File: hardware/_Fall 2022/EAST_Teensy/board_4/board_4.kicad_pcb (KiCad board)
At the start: 2 copper layers, 7 parts, among them J1 Conn_01x04, J2 Conn_02x08_Odd_Even, U1 Teensy4.1

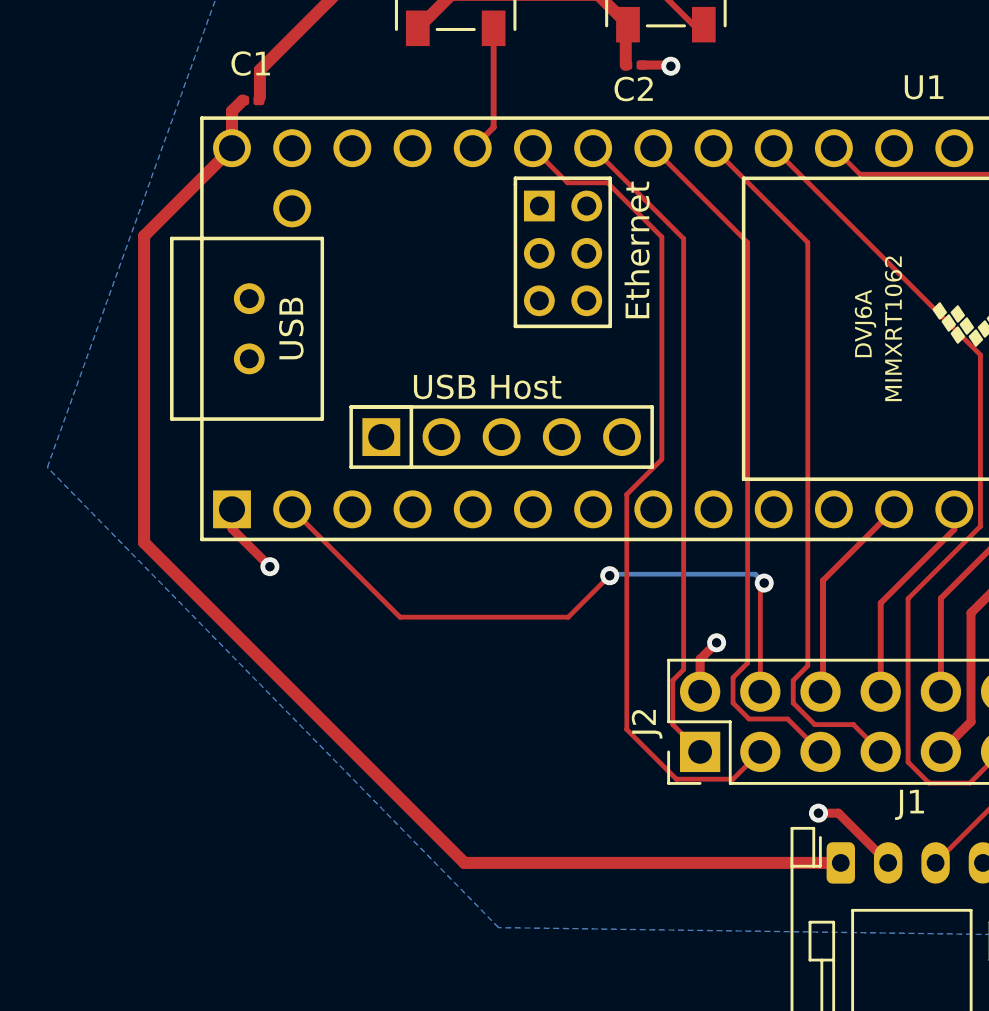
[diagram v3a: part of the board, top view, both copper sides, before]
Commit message: Edit layout of board 4
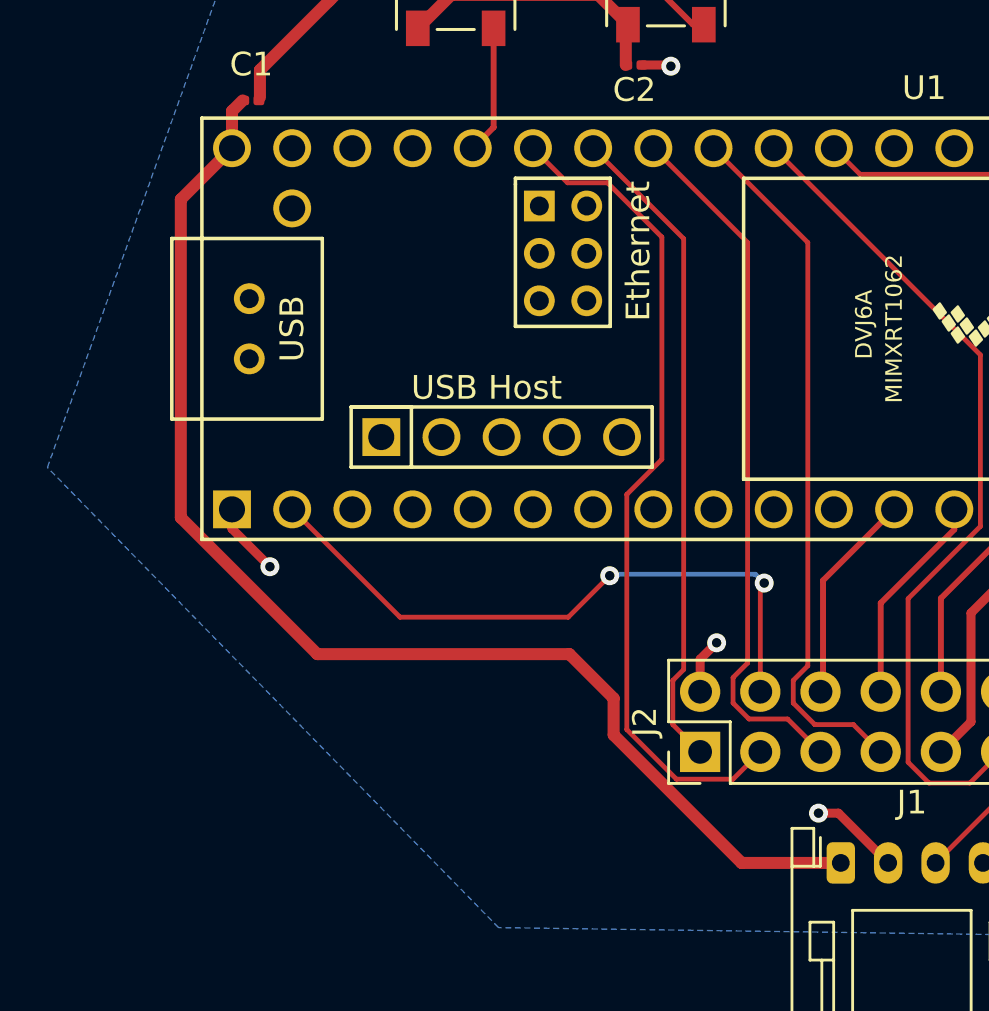
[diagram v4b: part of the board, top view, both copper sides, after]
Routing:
- net /V_BATT: track 55.4 -> 53.5 mm
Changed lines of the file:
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@@
   (gr_line (start 122.698438 153) (end 173.1 153) (layer "Dwgs.User") (width 0.2))
   (gr_circle (center 175.394719 140.299534) (end 173.565919 140.299534) (layer "Dwgs.User") (width 0.2) (fill none))
-  (segment (start 115.7 131.63) (end 115.7 118.7) (width 0.508) (layer "F.Cu") (net 1))
-  (segment (start 145.1 145.15) (end 129.22 145.15) (width 0.508) (layer "F.Cu") (net 1))
-  (segment (start 129.22 145.15) (end 115.7 131.63) (width 0.508) (layer "F.Cu") (net 1))
+  (segment (start 145.1 145.15) (end 140.914263 145.15) (width 0.508) (layer "F.Cu") (net 1))
+  (segment (start 135.5144 138.2044) (end 133.65 136.34) (width 0.508) (layer "F.Cu") (net 1))
+  (segment (start 140.914263 145.15) (end 135.5144 139.750137) (width 0.508) (layer "F.Cu") (net 1))
+  (segment (start 135.5144 139.750137) (end 135.5144 138.2044) (width 0.508) (layer "F.Cu") (net 1))
   (segment (start 119.41 113.426) (end 119.861 112.975) (width 0.508) (layer "F.Cu") (net 1))
-  (segment (start 115.7 118.7) (end 119.41 114.99) (width 0.508) (layer "F.Cu") (net 1))
+  (segment (start 123.012 136.34) (end 117.25 130.578) (width 0.508) (layer "F.Cu") (net 1))
+  (segment (start 133.65 136.34) (end 123.012 136.34) (width 0.508) (layer "F.Cu") (net 1))
   (segment (start 119.41 114.99) (end 119.41 113.426) (width 0.508) (layer "F.Cu") (net 1))
+  (segment (start 117.25 130.578) (end 117.25 117.15) (width 0.508) (layer "F.Cu") (net 1))
+  (segment (start 117.25 117.15) (end 119.41 114.99) (width 0.508) (layer "F.Cu") (net 1))
   (segment (start 136.12 104.8775) (end 135.0685 103.826) (width 0.508) (layer "F.Cu") (net 2))
   (segment (start 123.525 107.335) (end 123.16 106.97) (width 0.508) (layer "F.Cu") (net 2))

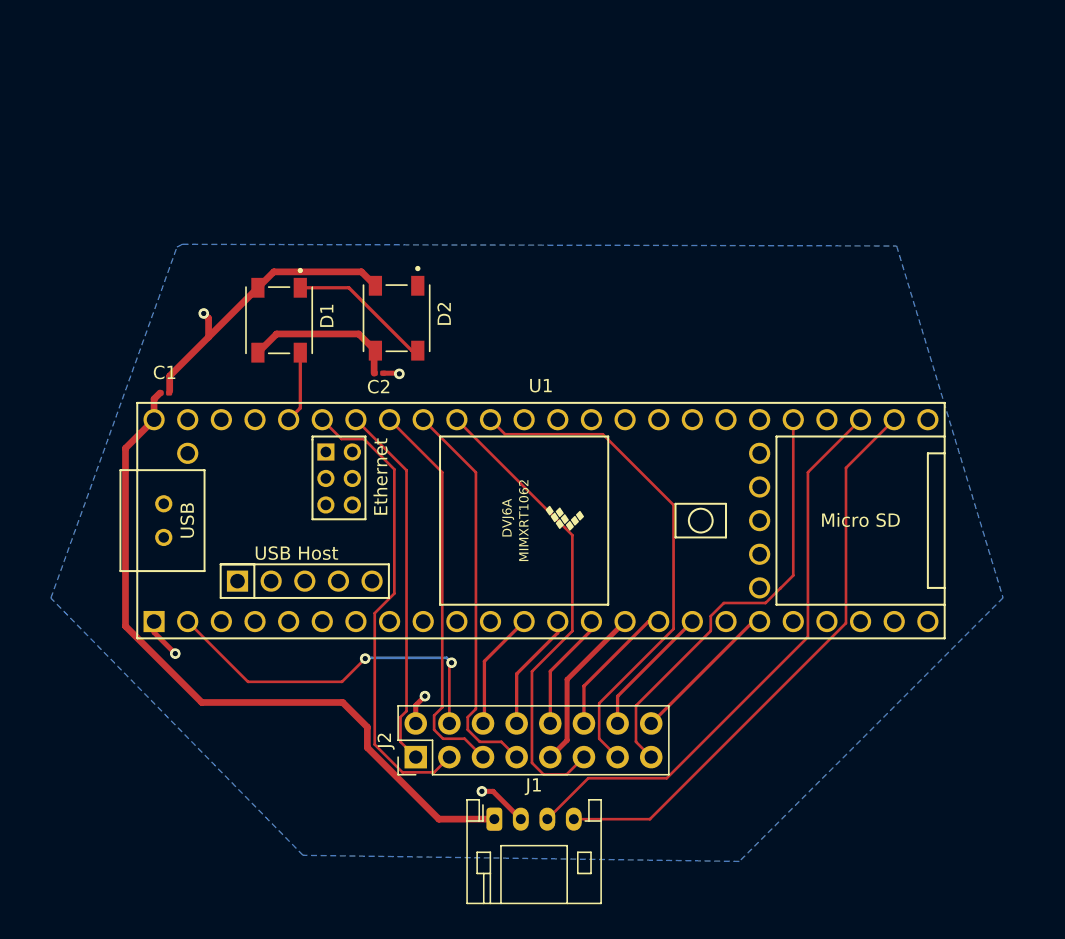
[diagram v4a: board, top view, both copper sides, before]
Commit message: Update EAST connectors
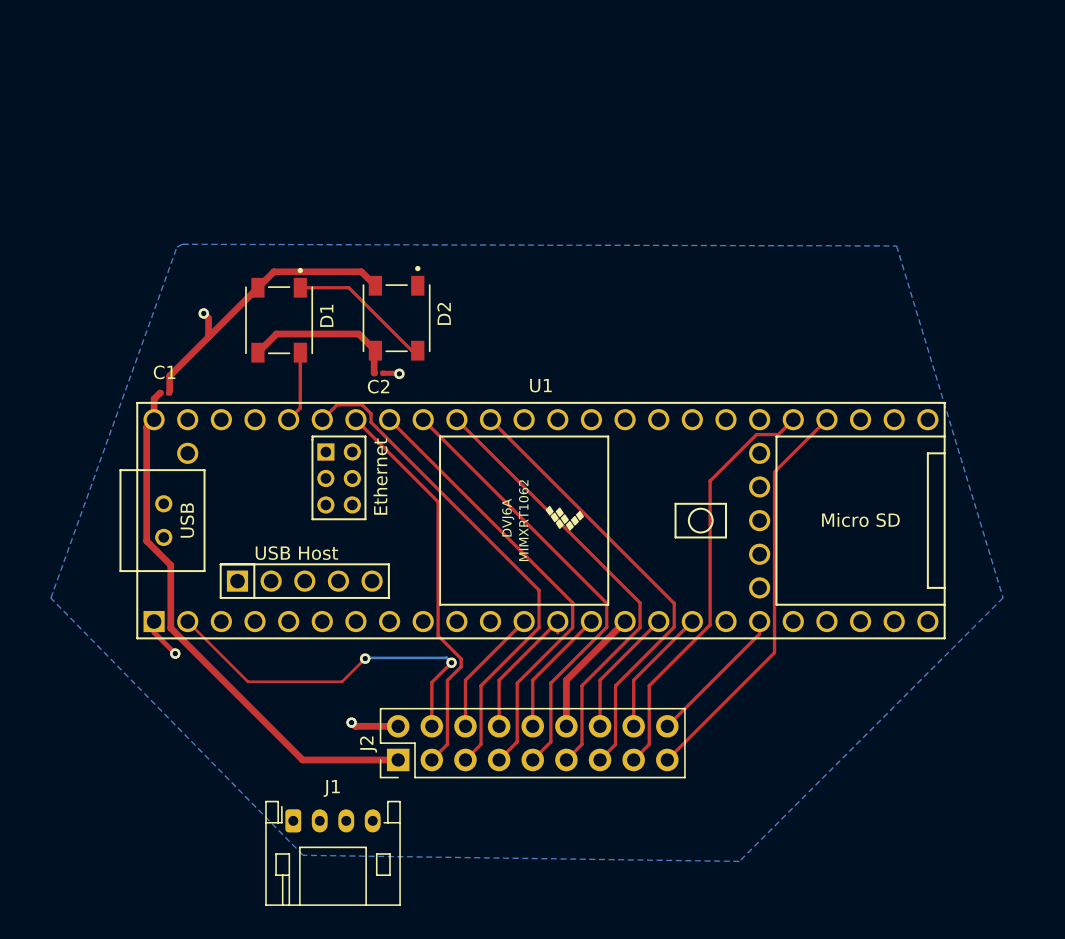
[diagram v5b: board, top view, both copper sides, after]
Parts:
- J2: value Conn_02x08_Odd_Even -> Conn_02x09_Odd_Even; footprint Connector_PinHeader_2.54mm:PinHeader_2x08_P2.54mm_Vertical -> Connector_PinHeader_2.54mm:PinHeader_2x09_P2.54mm_Vertical
- moved J1 15.2 mm to (129.9, 145.3)
- moved J2 1.34 mm to (137.8, 140.7)
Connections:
- J2 pad 1: /RX 2 -> /V_BATT
- J2 pad 12: /SCL 2 -> /3.3V
- J2 pad 14: /SDA 2 -> /SCL 2
- J2 pad 16: /SCK 1 -> /SDA 2
- J2 pad 3: /TX 2 -> /RX 2
- J2 pad 5: /SCL 1 -> /TX 2
- J2 pad 7: /SDA 1 -> /SCL 1
- J2 pad 9: /3.3V -> /SDA 1
- U1 pad 28: unconnected-(U1-Pad28) -> /CS 4
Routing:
- net /TX 0: track 43.5 -> 0.00 mm
- net /RX 0: track 43.4 -> 0.00 mm
- net /CS 4: track 0.00 -> 30.7 mm
- net /V_BATT: track 53.5 -> 40.2 mm
- net /RX 1: track 38.4 -> 33.8 mm
- net /SDA 1: track 29.9 -> 33.7 mm
- net /SCL 1: track 29.9 -> 33.7 mm
- net /3.3V: track 12.6 -> 9.74 mm
- net /TX 2: track 35.4 -> 38.1 mm
- net GND: track 32.8 -> 30.3 mm, vias 5 -> 4
- net /RX 2: track 27.7 -> 29.9 mm
- net /TX 1: track 35.6 -> 33.7 mm
- net /MOSI 1: track 8.98 -> 10.6 mm
- net /MISO 1: track 8.98 -> 10.4 mm
- net /CS 3: track 32.7 -> 31.6 mm
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
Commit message: Add final traces
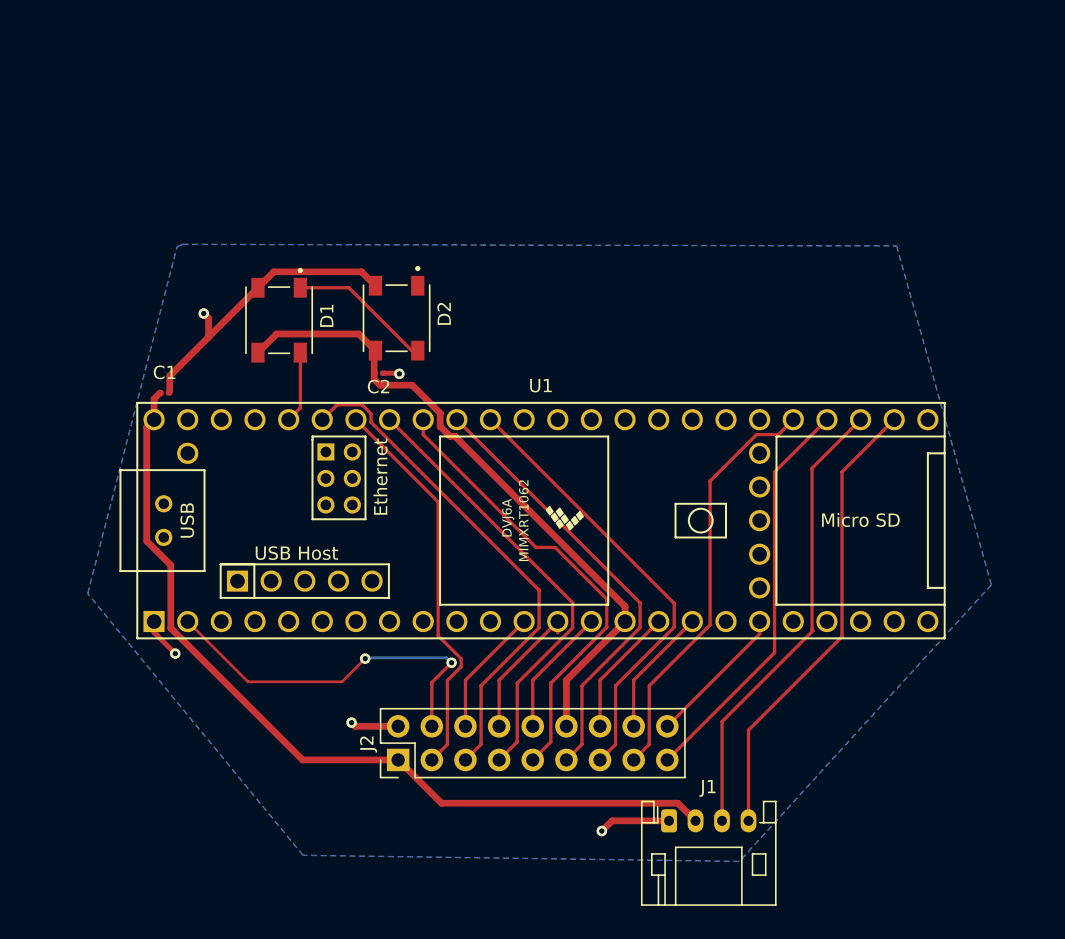
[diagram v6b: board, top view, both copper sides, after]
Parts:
- moved J1 28.4 mm to (158.3, 145.3)
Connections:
- C2 pad 2: +3.3V -> /3.3V
- D1 pad 3: +3.3V -> /3.3V
- D2 pad 3: +3.3V -> /3.3V
- J1 pad 1: /V_BATT -> GND
- J1 pad 2: GND -> /V_BATT
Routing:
- net /3.3V: track 9.74 -> 49.7 mm
- net /TX 0: track 0.00 -> 34.8 mm
- net /RX 0: track 0.00 -> 34.7 mm
- net /V_BATT: track 40.2 -> 64.6 mm
- net +3.3V: track 11.7 -> 0.00 mm
- net GND: track 30.3 -> 35.7 mm, vias 4 -> 5
- net /SDA 1: track 33.7 -> 34.6 mm

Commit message: Fix errors on TX/RX and added buzzer
Current state: Board 1 - need to check diodes; Board 4 - done; GPS- not showing layout traces, all need logos
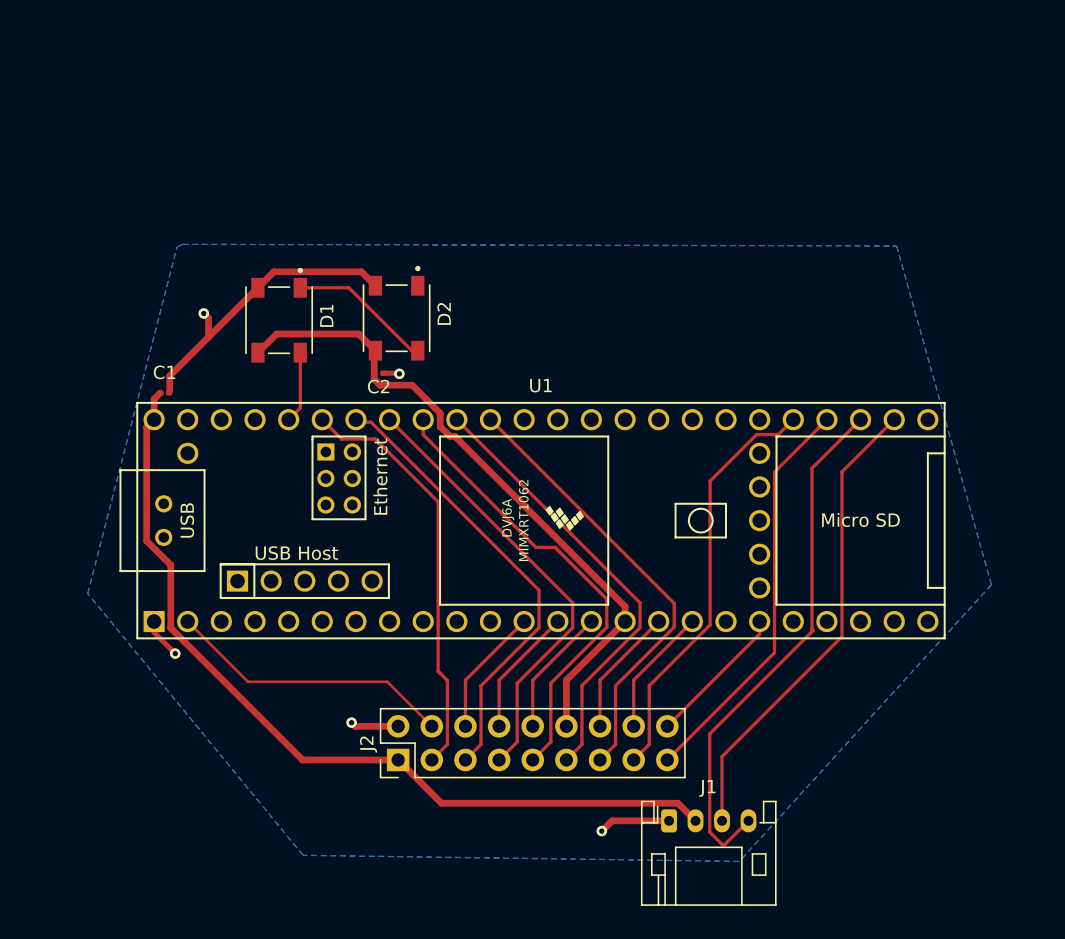
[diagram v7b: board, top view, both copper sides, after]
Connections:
- U1 pad 26: /TX 0 -> /RX 0
- U1 pad 27: /RX 0 -> /TX 0
- U1 pad 42: /RX 2 -> /TX 2
- U1 pad 43: /TX 2 -> /RX 2
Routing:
- net /CS 1: track 28.4 -> 21.7 mm, vias 2 -> 0
- net /TX 0: track 34.8 -> 40.0 mm
- net /TX 2: track 38.1 -> 34.3 mm
- net /RX 2: track 29.9 -> 31.6 mm
- net /RX 0: track 34.7 -> 35.7 mm
- net /MOSI 1: track 10.6 -> 9.74 mm
- net /MISO 1: track 10.4 -> 9.74 mm

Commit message: logos
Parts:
- added ?: LOGO, LOGO, F.Cu at (134.6, 149.9)
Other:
- board outline added: 76.2 x 66.7 mm
